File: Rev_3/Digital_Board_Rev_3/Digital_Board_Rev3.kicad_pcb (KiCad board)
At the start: 4 copper layers, 59.5 x 96.3 mm, 91 parts, among them J1 Conn_01x02_Male, J10 AudioJack3_Switch, J11 Conn_01x10_Female, J12 Barrel_Jack, J13 Conn_01x06_Female, J14 Conn_01x06_Female, J15 Conn_01x03_Male, J2 Conn_01x02_Male, J3 Conn_01x06_Male, J4 Conn_01x08_Female, J5 AudioJack3_Switch, J6 AudioJack3_Switch, J7 AudioJack3_Switch, J8 AudioJack3_Switch, J9 AudioJack3_Switch, K1 IM05, Q1 BSS83P, Q25 MMBT3904, SW1 SW_SPDT_MSM, SW2 SW_SPDT_MSM, SW3 SW_SPDT_MSM, U1 STM32F303R6Tx, U26 TLP222A-2, U27 NCP1117-3.3_SOT223, U28 TC7662Bx0A, Y1 8MHz

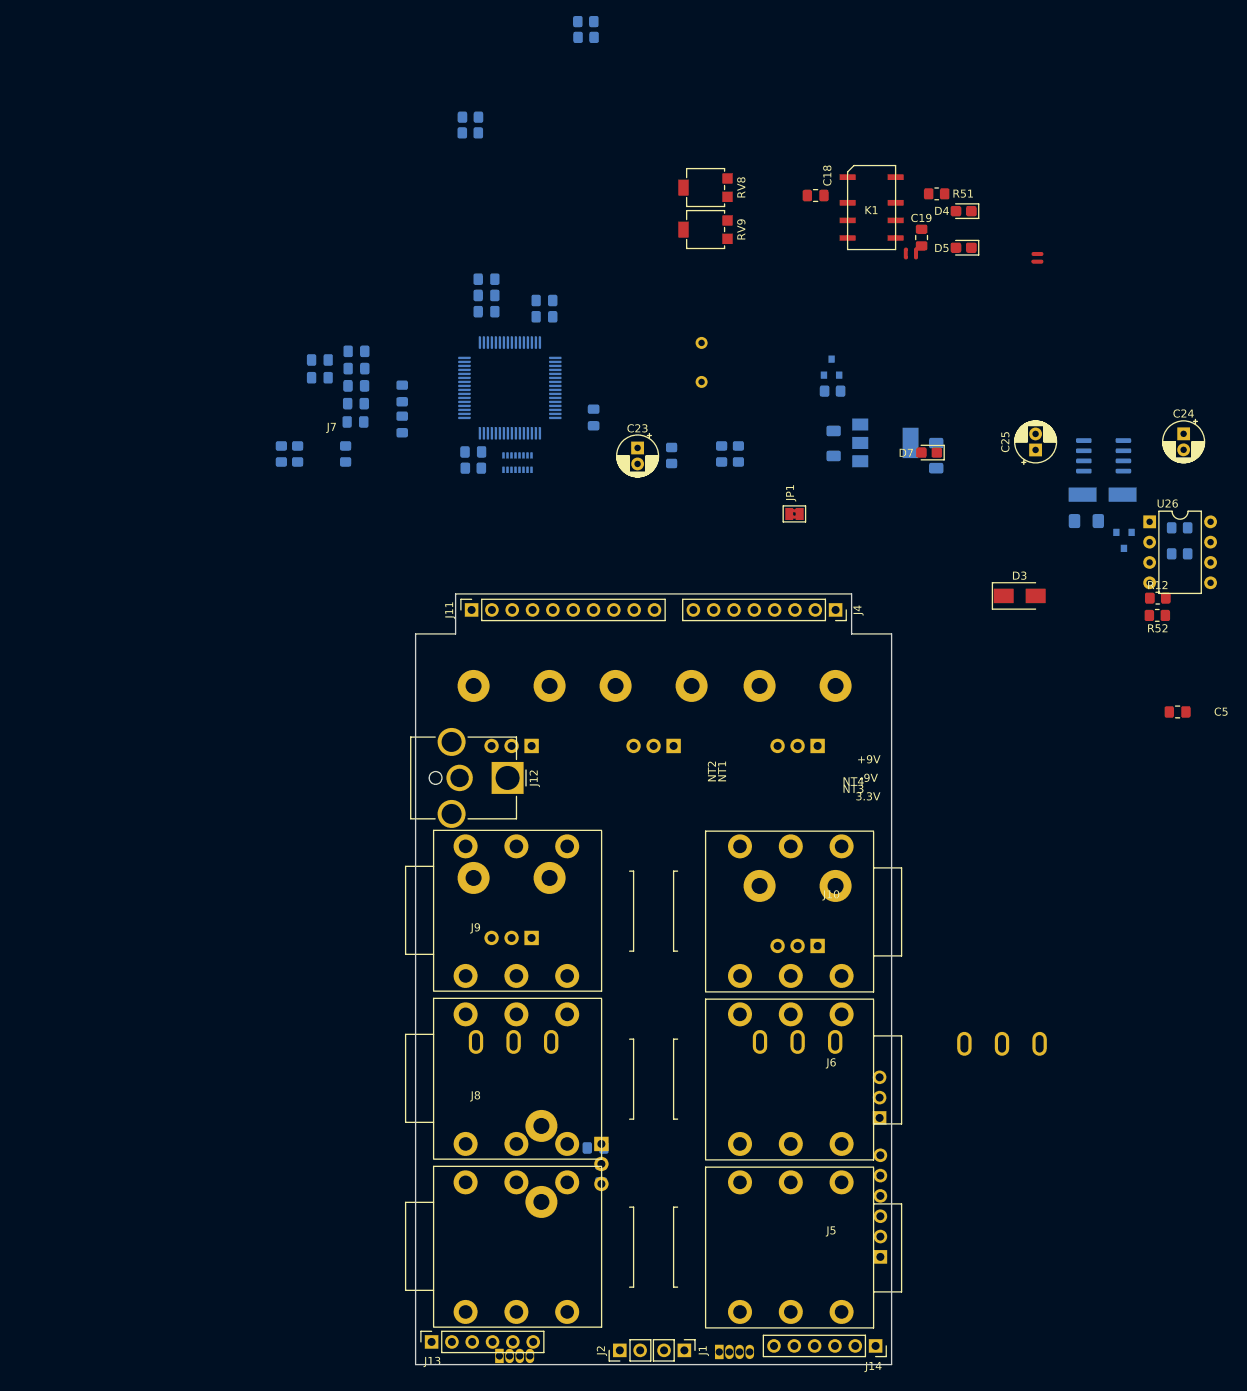
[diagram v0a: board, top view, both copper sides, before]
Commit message: Pivoting to Passive Jack Boards
Finalized layout for input/output Jack Boards, which are now completely passive and connected with board-to-board connectors. Schematics are not updated yet, just figuring out placement/dimensions.
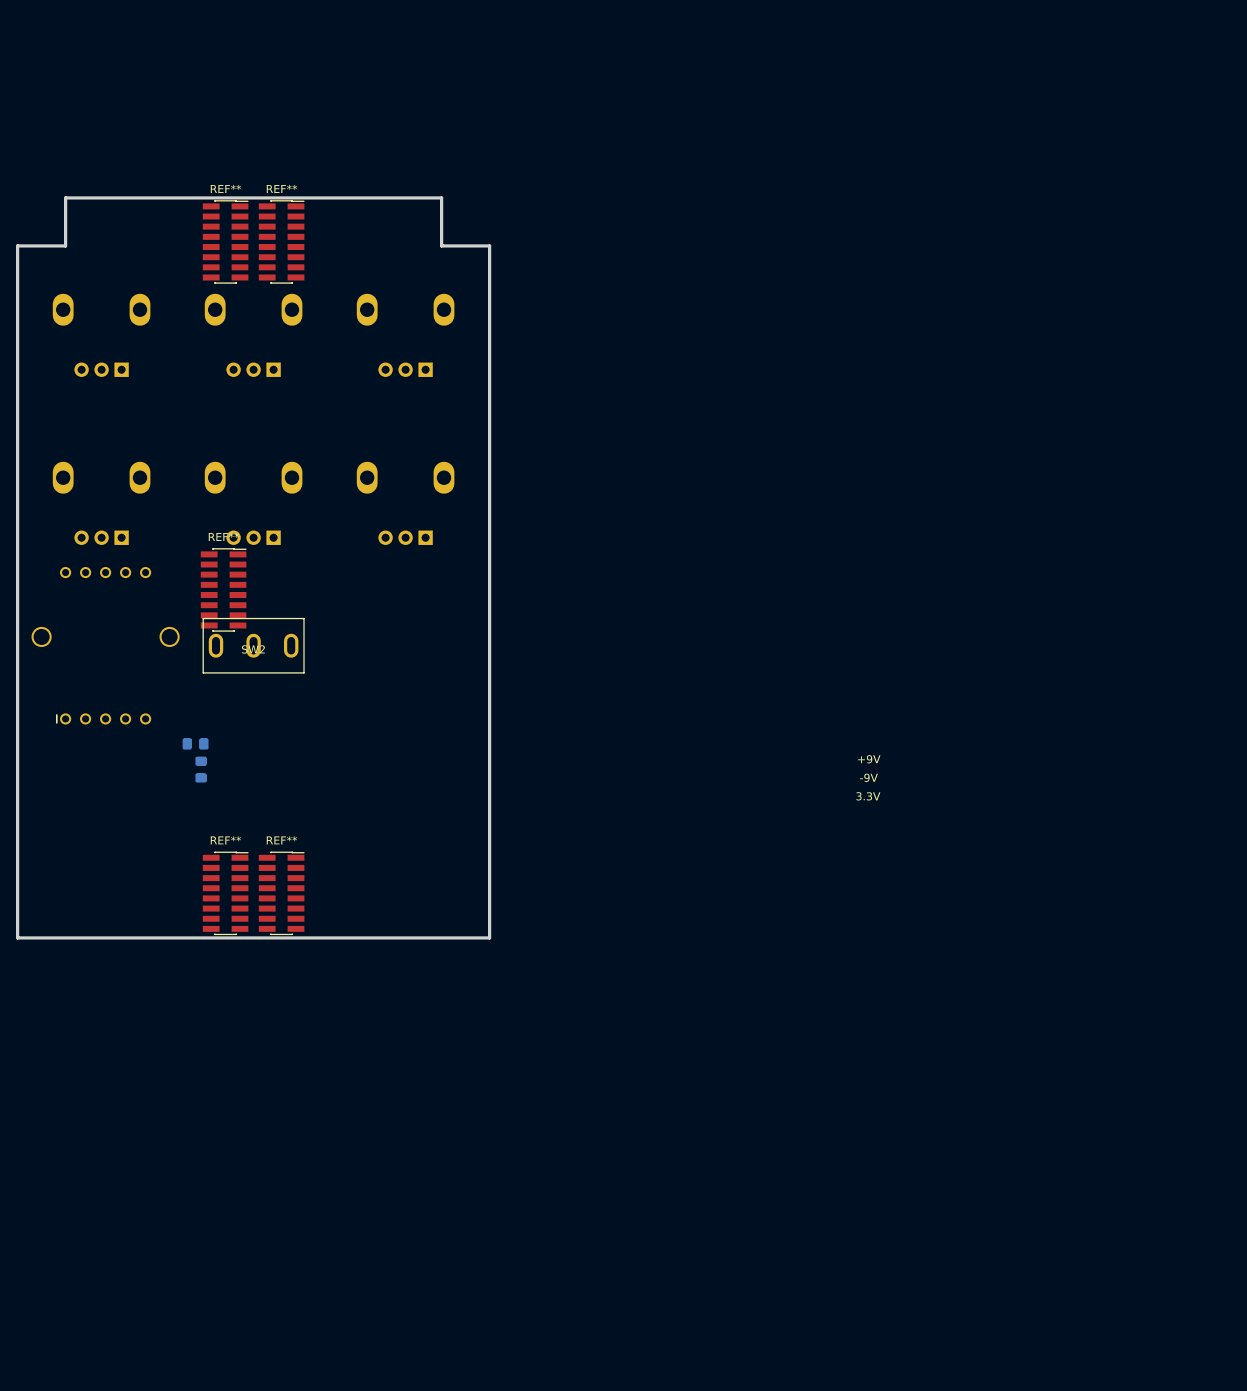
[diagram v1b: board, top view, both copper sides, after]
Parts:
- removed C1: 4.7u, Capacitor_SMD:C_0805_2012Metric_Pad1.18x1.45mm_HandSolder
- removed C11, C12, C13, C14, C15, C26: 100nF, Capacitor_SMD:C_0805_2012Metric_Pad1.18x1.45mm_HandSolder
- removed C16, C17, C20, C4, C5, C6, C7, C8: 100n, Capacitor_SMD:C_0805_2012Metric_Pad1.18x1.45mm_HandSolder
- removed C18, C19: 470n, Capacitor_SMD:C_0805_2012Metric_Pad1.18x1.45mm_HandSolder
- removed C2, C3: 18p, Capacitor_SMD:C_0805_2012Metric_Pad1.18x1.45mm_HandSolder
- removed C21, C22: 10u, Capacitor_SMD:C_1206_3216Metric_Pad1.33x1.80mm_HandSolder
- removed C23, C24, C25: 100uF, Capacitor_THT:CP_Radial_D5.0mm_P2.00mm
- removed D1, D2: LED_RGBA, LED_THT:LED_D5.0mm-4_RGB
- removed D3: B120-E3, Diode_SMD:D_SMA
- removed D4, D5, D7: LED_Small, LED_SMD:LED_0805_2012Metric_Castellated
- removed D6: D_Zener, Diode_SMD:D_SMA_Handsoldering
- removed F1: Polyfuse, Fuse:Fuse_1206_3216Metric_Pad1.42x1.75mm_HandSolder
- removed J1, J2: Conn_01x02_Male, Connector_PinHeader_2.54mm:PinHeader_1x02_P2.54mm_Vertical
- removed J10, J5, J6, J7, J8, J9: AudioJack3_Switch, Pinebox:Jack_0.25in_TRS_Switched
- removed J11: Conn_01x10_Female, Connector_PinSocket_2.54mm:PinSocket_1x10_P2.54mm_Vertical
- removed J12: Barrel_Jack, Connector_BarrelJack:BarrelJack_CUI_PJ-063AH_Horizontal_CircularHoles
- removed J13, J14: Conn_01x06_Female, Connector_PinSocket_2.54mm:PinSocket_1x06_P2.54mm_Vertical
- removed J15: Conn_01x03_Male, Connector_PinHeader_2.54mm:PinHeader_1x03_P2.54mm_Vertical
- removed J3: Conn_01x06_Male, Connector_PinHeader_2.54mm:PinHeader_1x06_P2.54mm_Vertical
- removed J4: Conn_01x08_Female, Connector_PinSocket_2.54mm:PinSocket_1x08_P2.54mm_Vertical
- removed JP1: Jumper, Jumper:SolderJumper-2_P1.3mm_Bridged2Bar_Pad1.0x1.5mm
- removed K1: IM05, Pinebox:Relay_DPDT_NL_TE_IM05GR
- removed NT1, NT2, NT3, NT4: Net-Tie_2, NetTie:NetTie-2_SMD_Pad0.5mm
- removed Q1: BSS83P, Package_TO_SOT_SMD:SOT-23
- removed Q25: MMBT3904, Package_TO_SOT_SMD:SOT-23
- removed R1, R8: 10k, Resistor_SMD:R_0805_2012Metric_Pad1.20x1.40mm_HandSolder
- removed R10, R11, R2, R3, R4, R5: 330, Resistor_SMD:R_0805_2012Metric_Pad1.20x1.40mm_HandSolder
- removed R12, R51, R6, R7: 1k, Resistor_SMD:R_0805_2012Metric_Pad1.20x1.40mm_HandSolder
- removed R50: 2.2k, Resistor_SMD:R_0805_2012Metric_Pad1.20x1.40mm_HandSolder
- removed R52: 470, Resistor_SMD:R_0805_2012Metric_Pad1.20x1.40mm_HandSolder
- removed R53, R54: 630, Resistor_SMD:R_0805_2012Metric_Pad1.20x1.40mm_HandSolder
- removed R9: 19.1k, Resistor_SMD:R_0805_2012Metric_Pad1.20x1.40mm_HandSolder
- removed RN1: R_Pack08, Resistor_SMD:R_Array_Convex_8x0602
- removed RV1, RV10, RV2, RV3, RV4, RV5: R_POT_TRIM, Pinebox:Potentiometer_9MM
- removed RV8, RV9: 100k, Potentiometer_SMD:Potentiometer_Bourns_3314G_Vertical
- removed SW1, SW3: SW_SPDT_MSM, Pinebox:SW_Toggle_SPDT
- removed U1: STM32F303R6Tx, Package_QFP:LQFP-64_10x10mm_P0.5mm
- removed U26: TLP222A-2, Package_DIP:DIP-8_W7.62mm
- removed U27: NCP1117-3.3_SOT223, Package_TO_SOT_SMD:SOT-223-3_TabPin2
- removed U28: TC7662Bx0A, Package_SO:SOIC-8_3.9x4.9mm_P1.27mm
- removed Y1: 8MHz, Crystal:Crystal_HC49-U_Vertical
- added REF**: PinSocket_2x08_P1.27mm_Vertical_SMD, Connector_PinSocket_1.27mm:PinSocket_2x08_P1.27mm_Vertical_SMD, F.Cu at (76.5, 56.5)
- added REF**: Potentiometer_9MM, BlackBox:Potentiometer_9MM, B.Cu at (61.0, 65.0)
- added REF**: Potentiometer_9MM, BlackBox:Potentiometer_9MM, B.Cu at (99.0, 86.0)
- added REF**: Potentiometer_9MM, BlackBox:Potentiometer_9MM, B.Cu at (61.0, 86.0)
- added REF**: Potentiometer_9MM, BlackBox:Potentiometer_9MM, B.Cu at (80.0, 65.0)
- added REF**: SR1712F-0106-20F0A-N9-N-027_ATW, BlackBox:SR1712F-0106-20F0A-N9-N-027_ATW, B.Cu at (61.5, 107.0)
- added REF**: PinSocket_2x08_P1.27mm_Vertical_SMD, Connector_PinSocket_1.27mm:PinSocket_2x08_P1.27mm_Vertical_SMD, F.Cu at (76.2, 100.0)
- added REF**: Input_Board_3D_TopJacks, g-art:Input_Board_3D_TopJacks, F.Cu at (80.0, 50.0)
- added REF**: Output_Board_3D_TopJacks, g-art:Output_Board_3D_TopJacks, F.Cu at (80.0, 50.0)
- added REF**: PinSocket_2x08_P1.27mm_Vertical_SMD, Connector_PinSocket_1.27mm:PinSocket_2x08_P1.27mm_Vertical_SMD, F.Cu at (83.5, 56.5)
- added REF**: PinSocket_2x08_P1.27mm_Vertical_SMD, Connector_PinSocket_1.27mm:PinSocket_2x08_P1.27mm_Vertical_SMD, F.Cu at (76.5, 137.9)
- added REF**: PinSocket_2x08_P1.27mm_Vertical_SMD, Connector_PinSocket_1.27mm:PinSocket_2x08_P1.27mm_Vertical_SMD, F.Cu at (83.5, 137.9)
- added REF**: Potentiometer_9MM, BlackBox:Potentiometer_9MM, B.Cu at (80.0, 86.0)
- added REF**: Potentiometer_9MM, BlackBox:Potentiometer_9MM, B.Cu at (99.0, 65.0)
- SW2: moved to F.Cu
- moved C10 71.1 mm to (72.8, 119.2)
- moved C9 71.1 mm to (73.4, 122.5)
- moved SW2 59.2 mm to (80.0, 107.0), turned to 0 degrees
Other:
- board size 59.5 x 96.3 mm -> 59 x 92.5 mm

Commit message: Added analog board back, switched to Jacks on Bottom
Added analog board mezzanine back to fit everything. Finalized decision on jack boards; jacks on bottom, wire to board connectors between jack boards and digital board. Tentative board outlines defined and scoped out component placement.
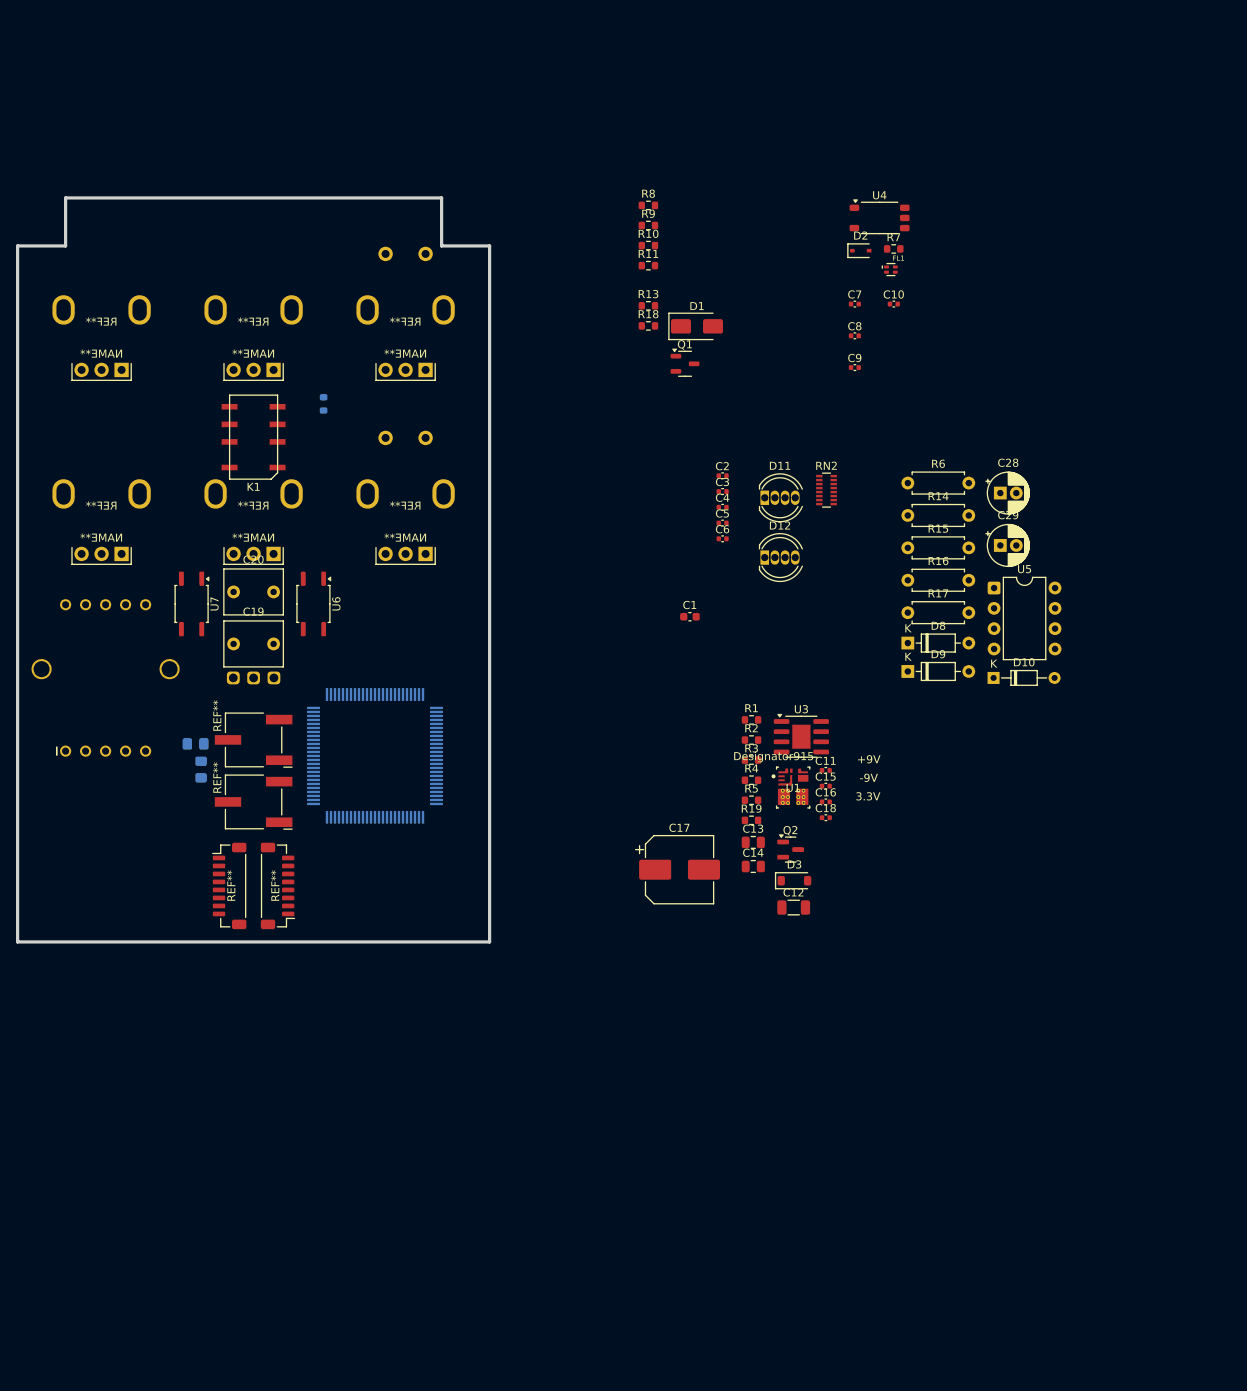
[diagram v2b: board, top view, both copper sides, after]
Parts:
- removed the REF** at (76.5, 56.5)
- removed the REF** at (76.2, 100.0)
- removed the REF** at (80.0, 50.0) (x2)
- removed the REF** at (83.5, 56.5)
- removed the REF** at (76.5, 137.9)
- removed the REF** at (83.5, 137.9)
- added C1: 2.2u, Capacitor_SMD:C_0603_1608Metric, F.Cu at (134.5, 103.3)
- added C10: 100n, Capacitor_SMD:C_0402_1005Metric, F.Cu at (160.0, 64.3)
- added C11: 33n, Capacitor_SMD:C_0402_1005Metric, F.Cu at (151.5, 122.6)
- added C12: 22u, Capacitor_SMD:C_1206_3216Metric, F.Cu at (147.5, 139.7)
- added C13: 10u, Capacitor_SMD:C_0805_2012Metric, F.Cu at (142.5, 131.6)
- added C14: 10u, Capacitor_SMD:C_0805_2012Metric, F.Cu at (142.5, 134.6)
- added C15: 1n, Capacitor_SMD:C_0402_1005Metric, F.Cu at (151.5, 124.5)
- added C16: 100n, Capacitor_SMD:C_0402_1005Metric, F.Cu at (151.5, 126.5)
- added C17: 100u, Capacitor_SMD:CP_Elec_8x6.2, F.Cu at (133.2, 135.0)
- added C18: 22p, Capacitor_SMD:C_0402_1005Metric, F.Cu at (151.5, 128.5)
- added C19: 1u, Capacitor_THT:C_Rect_L7.2mm_W5.5mm_P5.00mm_FKS2_FKP2_MKS2_MKP2, F.Cu at (77.5, 106.8)
- added C2: 100n, Capacitor_SMD:C_0402_1005Metric, F.Cu at (138.6, 85.7)
- added C20: 1u, Capacitor_THT:C_Rect_L7.2mm_W5.5mm_P5.00mm_FKS2_FKP2_MKS2_MKP2, F.Cu at (77.5, 100.2)
- added C28: 4.7u, Capacitor_THT:CP_Radial_D5.0mm_P2.00mm, F.Cu at (173.3, 87.9)
- added C29: 47u, Capacitor_THT:CP_Radial_D5.0mm_P2.00mm, F.Cu at (173.3, 94.4)
- added C3: 100n, Capacitor_SMD:C_0402_1005Metric, F.Cu at (138.6, 87.7)
- added C4: 100n, Capacitor_SMD:C_0402_1005Metric, F.Cu at (138.6, 89.7)
- added C5: 100n, Capacitor_SMD:C_0402_1005Metric, F.Cu at (138.6, 91.6)
- added C6: 100n, Capacitor_SMD:C_0402_1005Metric, F.Cu at (138.6, 93.6)
- added C7: 100n, Capacitor_SMD:C_0402_1005Metric, F.Cu at (155.2, 64.3)
- added C8: 100n, Capacitor_SMD:C_0402_1005Metric, F.Cu at (155.2, 68.2)
- added C9: 100n, Capacitor_SMD:C_0402_1005Metric, F.Cu at (155.2, 72.2)
- added D1: B120-E3, Diode_SMD:D_SMA, F.Cu at (135.4, 67.1)
- added D10: D_Zener, Diode_THT:D_DO-34_SOD68_P7.62mm_Horizontal, F.Cu at (172.5, 111.0)
- added D11: LED_RGBA, LED_THT:LED_D5.0mm-4_RGB, F.Cu at (143.9, 88.5)
- added D12: LED_RGBA, LED_THT:LED_D5.0mm-4_RGB, F.Cu at (143.9, 96.0)
- added D2: BAT54WS, Diode_SMD:D_SOD-323, F.Cu at (155.9, 57.6)
- added D3: MMSZ5236B-7-F, Diode_SMD:D_SOD-123, F.Cu at (147.6, 136.3)
- added D8: 1N914, Diode_THT:D_DO-35_SOD27_P7.62mm_Horizontal, F.Cu at (161.8, 106.6)
- added D9: 1N914, Diode_THT:D_DO-35_SOD27_P7.62mm_Horizontal, F.Cu at (161.8, 110.2)
- added FL1: ~, g-ind:FIL_EXC-24CB102U, F.Cu at (159.7, 60.0)
- added K1: IM05GR, g-rly:Relay_DPDT_TE_IM05GR, F.Cu at (80.0, 80.9)
- added Q1: MMBT3904, Package_TO_SOT_SMD:SOT-23-3, F.Cu at (133.9, 71.7)
- added Q2: DMP3099L, Package_TO_SOT_SMD:SOT-23, F.Cu at (147.1, 132.5)
- added R1: 1, Resistor_SMD:R_0603_1608Metric, F.Cu at (142.2, 116.2)
- added R10: 330, Resistor_SMD:R_0603_1608Metric, F.Cu at (129.3, 57.0)
- added R11: 1k, Resistor_SMD:R_0603_1608Metric, F.Cu at (129.3, 59.5)
- added R12: 1k, Resistor_SMD:R_0603_1608Metric, B.Cu at (88.8, 76.8)
- added R13: 1M, Resistor_SMD:R_0603_1608Metric, F.Cu at (129.3, 64.5)
- added R14: 100k, Resistor_THT:R_Axial_DIN0207_L6.3mm_D2.5mm_P7.62mm_Horizontal, F.Cu at (161.8, 90.7)
- added R15: 10k, Resistor_THT:R_Axial_DIN0207_L6.3mm_D2.5mm_P7.62mm_Horizontal, F.Cu at (161.8, 94.7)
- added R16: 47k, Resistor_THT:R_Axial_DIN0207_L6.3mm_D2.5mm_P7.62mm_Horizontal, F.Cu at (161.8, 98.8)
- added R17: 1k, Resistor_THT:R_Axial_DIN0207_L6.3mm_D2.5mm_P7.62mm_Horizontal, F.Cu at (161.8, 102.8)
- added R18: 1M, Resistor_SMD:R_0603_1608Metric, F.Cu at (129.3, 67.0)
- added R19: 10k, Resistor_SMD:R_0603_1608Metric, F.Cu at (142.2, 128.8)
- added R2: 180k, Resistor_SMD:R_0603_1608Metric, F.Cu at (142.2, 118.8)
- added R3: 43k, Resistor_SMD:R_0603_1608Metric, F.Cu at (142.2, 121.3)
- added R4: 68k, Resistor_SMD:R_0603_1608Metric, F.Cu at (142.2, 123.8)
- added R5: 15k, Resistor_SMD:R_0603_1608Metric, F.Cu at (142.2, 126.3)
- added R6: 3.3k, Resistor_THT:R_Axial_DIN0207_L6.3mm_D2.5mm_P7.62mm_Horizontal, F.Cu at (161.8, 86.6)
- added R7: 330, Resistor_SMD:R_0603_1608Metric, F.Cu at (160.0, 57.4)
- added R8: 4.7k, Resistor_SMD:R_0603_1608Metric, F.Cu at (129.3, 51.9)
- added R9: 330, Resistor_SMD:R_0603_1608Metric, F.Cu at (129.3, 54.4)
- added REF**: JST_SH_BM08B-SRSS-TB_1x08-1MP_P1.00mm_Vertical, Connector_JST:JST_SH_BM08B-SRSS-TB_1x08-1MP_P1.00mm_Vertical, F.Cu at (77.0, 137.0)
- added REF**: Footswitch_SPST, g-art:Footswitch_SPST, F.Cu at (99.0, 152.5)
- added REF**: TRIM_3361P-1-500GLF, g-pot:Potentiometer_Bourns_3361P_Vertical, F.Cu at (80.0, 126.5)
- added REF**: JST_SH_BM08B-SRSS-TB_1x08-1MP_P1.00mm_Vertical, Connector_JST:JST_SH_BM08B-SRSS-TB_1x08-1MP_P1.00mm_Vertical, F.Cu at (83.0, 137.0)
- added REF**: Input_Board_3D_BtmJacks, g-art:Input_Board_3D_BtmJacks, F.Cu at (80.0, 50.0)
- added REF**: TRIM_3361P-1-500GLF, g-pot:Potentiometer_Bourns_3361P_Vertical, F.Cu at (80.0, 118.8)
- added REF**: Footswitch_SPST, g-art:Footswitch_SPST, F.Cu at (61.0, 152.5)
- added REF**: Output_Board_3D_BtmJacks, g-art:Output_Board_3D_BtmJacks, F.Cu at (80.0, 50.0)
- added RN2: R_Pack08, Resistor_SMD:R_Array_Convex_8x0602, F.Cu at (151.6, 87.5)
- added U1: TPSM84338RCJR, g-reg:TI-RCJ0009A-MFG, F.Cu at (147.4, 124.8)
- added U2: STM32G474VBTx, Package_QFP:LQFP-100_14x14mm_P0.5mm, B.Cu at (95.2, 120.8)
- added U3: ADP7142ARDZ, Package_SO:SOIC-8-1EP_3.9x4.9mm_P1.27mm_EP2.29x3mm, F.Cu at (148.5, 118.3)
- added U4: TLP2361, Package_SO:SO-5-6_4.55x3.7mm_P1.27mm, F.Cu at (158.2, 53.5)
- added U5: OPA2134, Package_DIP:DIP-8_W7.62mm, F.Cu at (172.6, 99.8)
- added U6: TLP170AM, Package_SO:SO-4_4.4x3.9mm_P2.54mm, F.Cu at (87.5, 101.8)
- added U7: TLP170AM, Package_SO:SO-4_4.4x3.9mm_P2.54mm, F.Cu at (72.2, 101.8)
- REF** (x2): value Potentiometer_9MM -> Potentiometer_11MM_1-Gang_Bourns_PRS11R-4xxF-S; footprint BlackBox:Potentiometer_9MM -> g-pot:Potentiometer_11MM_1-Gang_Bourns_PRS11R-4xxF-S
- REF** (x4): value Potentiometer_9MM -> Potentiometer_11MM_1-Gang_Bourns_PRS11R-4xxF-N; footprint BlackBox:Potentiometer_9MM -> g-pot:Potentiometer_11MM_1-Gang_Bourns_PRS11R-4xxF-N
- REF**: footprint BlackBox:SR1712F-0106-20F0A-N9-N-027_ATW -> g-swi:SR1712F-0106-20F0A-N9-N-027_ATW
- SW2: footprint Pinebox:SW_Toggle_SPDT -> g-swi:SW_TOGGLE_ALPHA-200_SUBMINI_SPDT_PC-PINS; moved to B.Cu
- moved REF** 4.03 mm to (61.5, 111.0)
- moved SW2 4.03 mm to (80.0, 111.0)
- moved REF** 2.03 mm to (99.0, 88.0)
- moved REF** 2.03 mm to (61.0, 88.0)
- moved REF** 2.03 mm to (80.0, 88.0)
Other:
- board size 59 x 92.5 mm -> 59 x 93 mm
